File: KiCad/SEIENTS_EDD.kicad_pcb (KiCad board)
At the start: 2 copper layers, 127.1 x 110 mm, 94 parts, among them IC1 A3144EUA, J1 Conn_01x02_Pin, J201 Screw_Terminal_01x04, J3 Screw_Terminal_01x05, J4 Screw_Terminal_01x02, J7 DE9_Socket, J8 DE9_Pins, M4 Motor_DC, M5 Motor_DC, M6 Motor_DC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

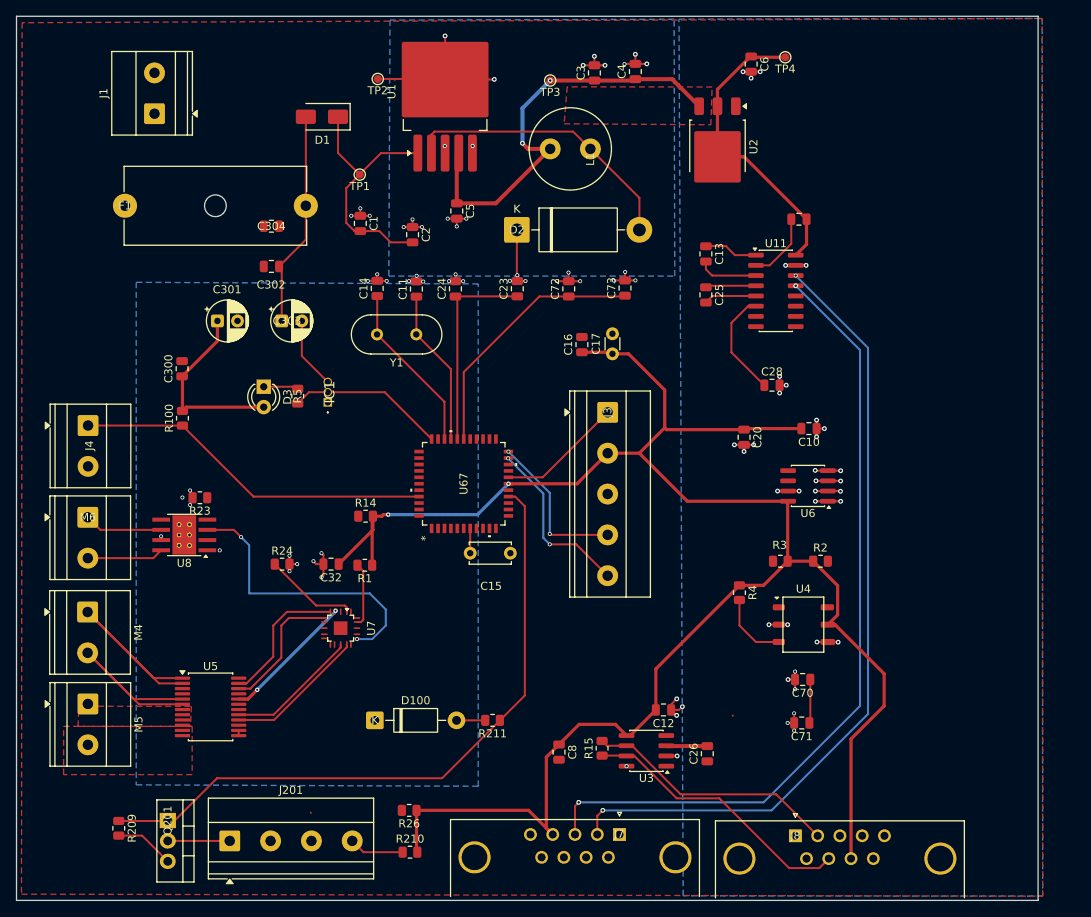
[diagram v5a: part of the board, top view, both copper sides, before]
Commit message: Modificació al routing
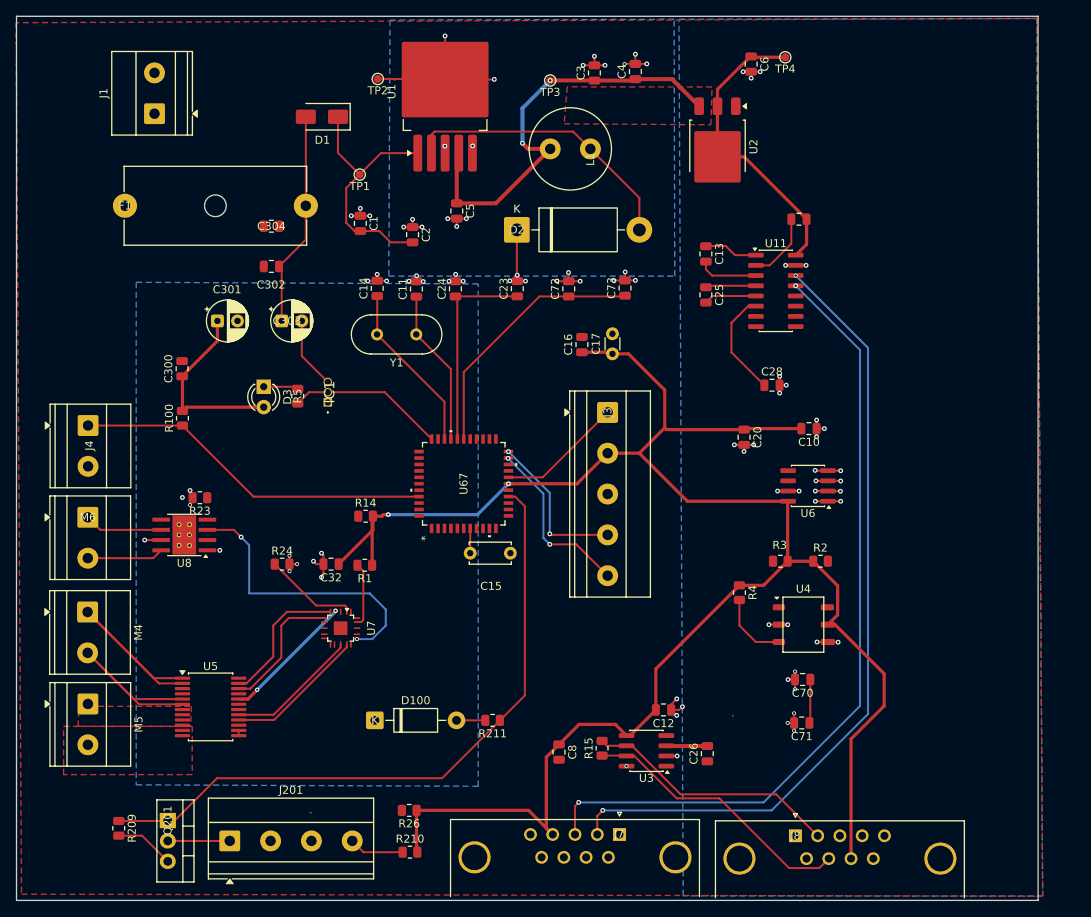
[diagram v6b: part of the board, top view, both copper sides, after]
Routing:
- net GND: track 167.7 -> 168.9 mm
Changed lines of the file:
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@@
 	)
 	(segment
-		(start 128.38 46.225)
-		(end 128.38 45.38)
-		(width 0.25)
-		(layer "F.Cu")
-		(net 1)
-	)
-	(segment
 		(start 174.6 80.5)
 		(end 174.6 81.515)
@@
 	)
 	(segment
+		(start 93.05 94.37)
+		(end 91 94.37)
+		(width 0.25)
+		(layer "F.Cu")
+		(net 1)
+	)
+	(segment
 		(start 128.305 37)
 		(end 128.38 37.075)
@@
 	(via
 		(at 123.225 55.425)
-		(size 0.5)
+		(size 0.6)
 		(drill 0.3)
 		(layers "F.Cu" "B.Cu")
@@
 	(via
 		(at 124.832599 61.482599)
-		(size 0.5)
+		(size 0.6)
 		(drill 0.3)
 		(layers "F.Cu" "B.Cu")
@@
 	(via
 		(at 152.057599 62.062599)
-		(size 0.5)
+		(size 0.6)
 		(drill 0.3)
 		(layers "F.Cu" "B.Cu")
@@
 	(via
 		(at 121.107599 62.132599)
-		(size 0.5)
+		(size 0.6)
 		(drill 0.3)
 		(layers "F.Cu" "B.Cu")
@@
 	(via
 		(at 131.025 54.375)
-		(size 0.5)
+		(size 0.6)
 		(drill 0.3)
 		(layers "F.Cu" "B.Cu")
@@
 	)
 	(via
-		(at 93.045 93.9)
-		(size 0.5)
+		(at 91 94.37)
+		(size 0.6)
 		(drill 0.3)
 		(layers "F.Cu" "B.Cu")
@@
 	(via
 		(at 129.83 55.35)
-		(size 0.5)
+		(size 0.6)
 		(drill 0.3)
 		(layers "F.Cu" "B.Cu")
@@
 	(via
 		(at 119 54.025)
-		(size 0.5)
+		(size 0.6)
 		(drill 0.3)
 		(layers "F.Cu" "B.Cu")
@@
 	(via
 		(at 125.657599 62.207599)
-		(size 0.5)
+		(size 0.6)
 		(drill 0.3)
 		(layers "F.Cu" "B.Cu")
@@
 	(via
 		(at 131.8 45.325)
-		(size 0.5)
+		(size 0.6)
 		(drill 0.3)
 		(layers "F.Cu" "B.Cu")
@@
 	(via
 		(at 128.7 54.375)
-		(size 0.5)
+		(size 0.6)
 		(drill 0.3)
 		(layers "F.Cu" "B.Cu")
@@
 	(via
 		(at 128.35 45.35)
-		(size 0.5)
+		(size 0.6)
 		(drill 0.3)
 		(layers "F.Cu" "B.Cu")
@@
 	(via
 		(at 113 99)
-		(size 0.5)
+		(size 0.6)
 		(drill 0.3)
 		(layers "F.Cu" "B.Cu")
@@
 	(via
 		(at 149.382599 62.087599)
-		(size 0.5)
+		(size 0.6)
 		(drill 0.3)
 		(layers "F.Cu" "B.Cu")
@@
 	(via
 		(at 137.357599 61.412599)
-		(size 0.5)
+		(size 0.6)
 		(drill 0.3)
 		(layers "F.Cu" "B.Cu")
@@
 	(via
 		(at 116.7 54.025)
-		(size 0.5)
+		(size 0.6)
 		(drill 0.3)
 		(layers "F.Cu" "B.Cu")
@@
 	(via
 		(at 96.645 88.2)
-		(size 0.5)
+		(size 0.6)
 		(drill 0.3)
 		(layers "F.Cu" "B.Cu")
@@
 	(via
 		(at 119.932599 61.307599)
-		(size 0.5)
+		(size 0.6)
 		(drill 0.3)
 		(layers "F.Cu" "B.Cu")
@@
 	(via
 		(at 145.182599 62.162599)
-		(size 0.5)
+		(size 0.6)
 		(drill 0.3)
 		(layers "F.Cu" "B.Cu")
@@
 	(via
 		(at 142.282599 62.137599)
-		(size 0.5)
+		(size 0.6)
 		(drill 0.3)
 		(layers "F.Cu" "B.Cu")
@@
 	(via
 		(at 143.732599 61.087599)
-		(size 0.5)
+		(size 0.6)
 		(drill 0.3)
 		(layers "F.Cu" "B.Cu")
@@
 	(via
 		(at 118.757599 62.132599)
-		(size 0.5)
+		(size 0.6)
 		(drill 0.3)
 		(layers "F.Cu" "B.Cu")
@@
 	(via
 		(at 130.632599 62.162599)
-		(size 0.5)
+		(size 0.6)
 		(drill 0.3)
 		(layers "F.Cu" "B.Cu")
@@
 	(via
 		(at 150.782599 61.012599)
-		(size 0.5)
+		(size 0.6)
 		(drill 0.3)
 		(layers "F.Cu" "B.Cu")
@@
 	(via
 		(at 117.83 53.1)
-		(size 0.5)
+		(size 0.6)
 		(drill 0.3)
 		(layers "F.Cu" "B.Cu")
@@
 	(via
 		(at 128.857599 62.162599)
-		(size 0.5)
+		(size 0.6)
 		(drill 0.3)
 		(layers "F.Cu" "B.Cu")
@@
 	(via
 		(at 138.382599 62.137599)
-		(size 0.5)
+		(size 0.6)
 		(drill 0.3)
 		(layers "F.Cu" "B.Cu")
@@
 	(via
 		(at 100.345 95.65)
-		(size 0.5)
+		(size 0.6)
 		(drill 0.3)
 		(layers "F.Cu" "B.Cu")
@@
 	(via
 		(at 123.882599 62.157599)
-		(size 0.5)
+		(size 0.6)
 		(drill 0.3)
 		(layers "F.Cu" "B.Cu")
@@
 	(via
 		(at 95.695 89.075)
-		(size 0.5)
+		(size 0.6)
 		(drill 0.3)
 		(layers "F.Cu" "B.Cu")
@@
 	(via
 		(at 124.33 54.475)
-		(size 0.5)
+		(size 0.6)
 		(drill 0.3)
 		(layers "F.Cu" "B.Cu")
@@
 	(via
 		(at 112 97)
-		(size 0.5)
+		(size 0.6)
 		(drill 0.3)
 		(layers "F.Cu" "B.Cu")
@@
 	(via
 		(at 129.682599 61.312599)
-		(size 0.5)
+		(size 0.6)
 		(drill 0.3)
 		(layers "F.Cu" "B.Cu")
@@
 	(via
 		(at 125.5 55.425)
-		(size 0.5)
+		(size 0.6)
 		(drill 0.3)
 		(layers "F.Cu" "B.Cu")
@@
 	(via
 		(at 113 96)
-		(size 0.5)
+		(size 0.6)
 		(drill 0.3)
 		(layers "F.Cu" "B.Cu")
@@
 	(via
 		(at 136.432599 62.112599)
-		(size 0.5)
+		(size 0.6)
 		(drill 0.3)
 		(layers "F.Cu" "B.Cu")
@@
 	(via
 		(at 136.262599 87.3626)
-		(size 0.55)
+		(size 0.6)
 		(drill 0.25)
 		(layers "F.Cu" "B.Cu")
@@
 	(via
 		(at 121.3 91.2)
-		(size 0.55)
+		(size 0.6)
 		(drill 0.25)
 		(layers "F.Cu" "B.Cu")
@@
 	(via
 		(at 136.262599 83.3626)
-		(size 0.5)
+		(size 0.6)
 		(drill 0.3)
 		(layers "F.Cu" "B.Cu")
@@
 	(via
 		(at 141.4 93.6)
-		(size 0.5)
+		(size 0.6)
 		(drill 0.3)
 		(layers "F.Cu" "B.Cu")
@@
 	(via
 		(at 141.4 94.9)
-		(size 0.5)
+		(size 0.6)
 		(drill 0.3)
 		(layers "F.Cu" "B.Cu")
@@
 	(via
 		(at 136.220657 84.204543)
-		(size 0.5)
+		(size 0.6)
 		(drill 0.3)
 		(layers "F.Cu" "B.Cu")
@@
 	(via
 		(at 103 94)
-		(size 0.5)
+		(size 0.6)
 		(drill 0.3)
 		(layers "F.Cu" "B.Cu")
@@
 		(polygon
 			(pts
-				(xy 75.75 30) (xy 75.675 138.425) (xy 202.725 138.675) (xy 202.675 29.475)
+				(xy 75 30) (xy 75.675 138.425) (xy 202.725 138.675) (xy 202 29.475)
 			)
 		)
@@
 		(polygon
 			(pts
-				(xy 157.475 29.575) (xy 202.675 29.475) (xy 202.725 138.675) (xy 158 138.625)
+				(xy 157.475 29.575) (xy 202 29.475) (xy 202.725 138.675) (xy 158 138.625)
 			)
 		)

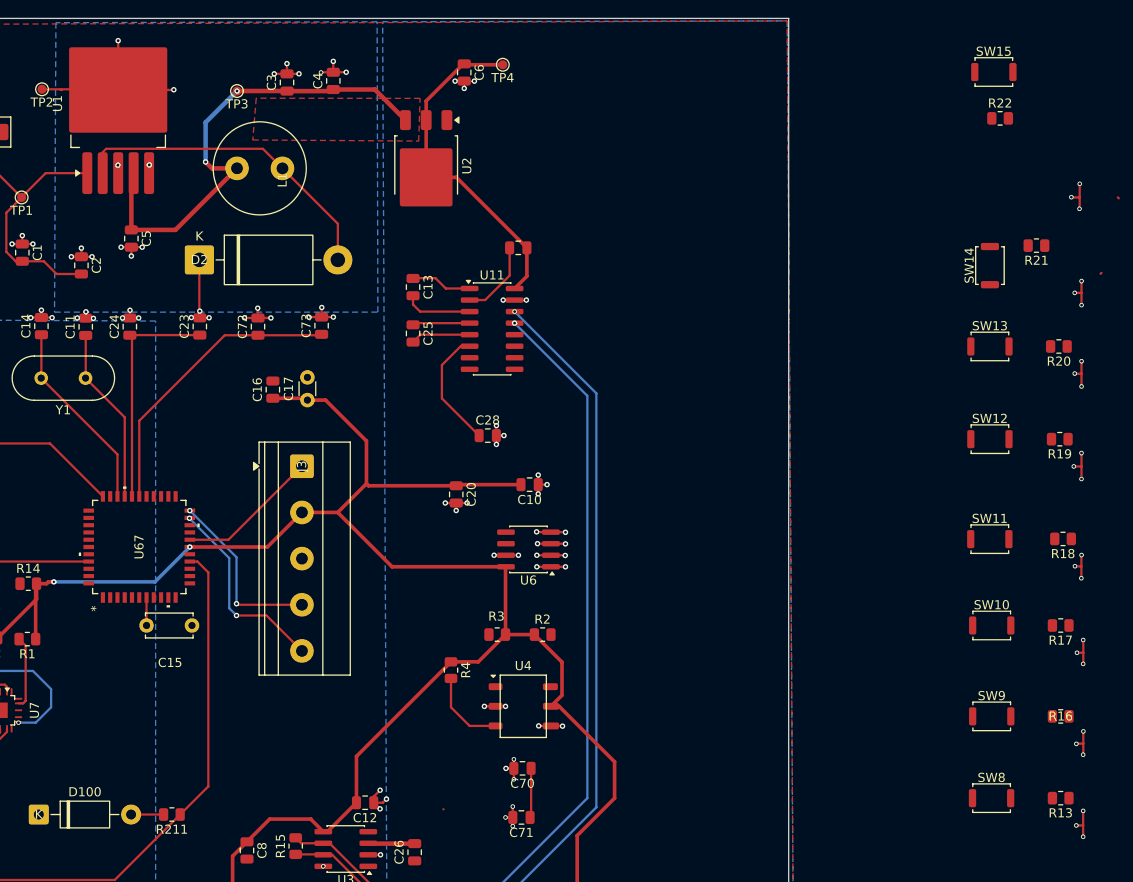
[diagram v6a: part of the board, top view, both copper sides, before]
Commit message: Modificació al routing
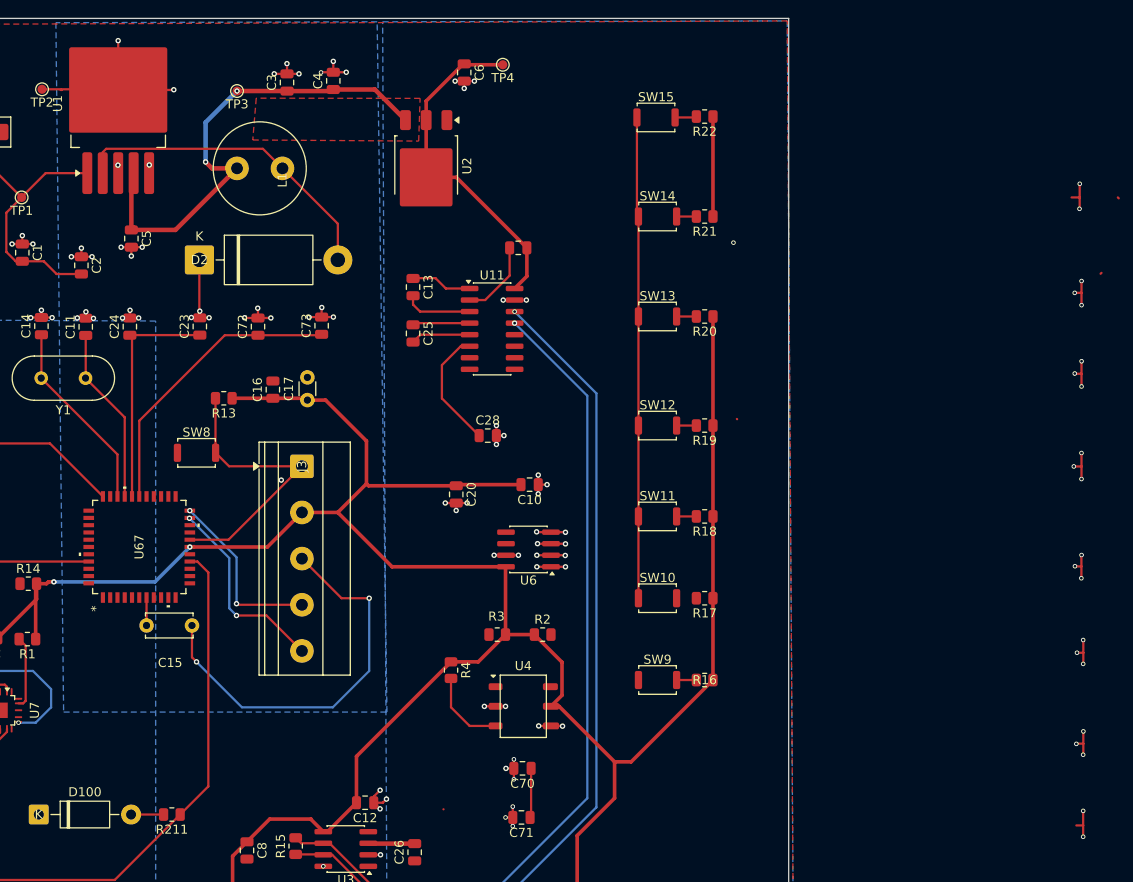
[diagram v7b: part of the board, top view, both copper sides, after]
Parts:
- moved R13 102.1 mm to (140.0, 71.0)
- moved SW8 95.4 mm to (137.0, 77.0)
- moved R18 39.5 mm to (192.9, 84.0)
- moved R16 39.4 mm to (192.9, 102.0)
- moved R17 39.3 mm to (192.9, 93.0)
- moved R20 39.1 mm to (192.9, 62.0)
- moved R19 39.1 mm to (192.9, 74.0)
- moved SW15 37.5 mm to (187.6, 40.1)
- moved SW9 37.0 mm to (187.7, 102.0)
- moved SW14 37.0 mm to (187.7, 51.0), turned to 0 degrees
- moved SW10 36.9 mm to (187.7, 93.0)
- moved SW13 36.7 mm to (187.7, 62.0)
- moved SW11 36.6 mm to (187.7, 84.0)
- moved R21 36.6 mm to (192.9, 51.0)
- moved SW12 36.6 mm to (187.7, 74.0)
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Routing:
- net GND: track 168.9 -> 266.0 mm, vias 111 -> 113
- net +3.3V: track 319.9 -> 389.9 mm
- net Net-(J3-Pin_1): track 15.7 -> 31.8 mm
- net BTN_TEMP_UP: track 0.14 -> 2.53 mm
- net BTN_REC_FWD: track 0.00 -> 2.18 mm
- net BTN_REC_BWD: track 0.14 -> 2.32 mm
- net BTN_POS_FWD: track 0.00 -> 2.18 mm
- net BTN_ALT_UP: track 0.00 -> 2.18 mm
- net BTN_ALT_DN: track 0.00 -> 2.18 mm

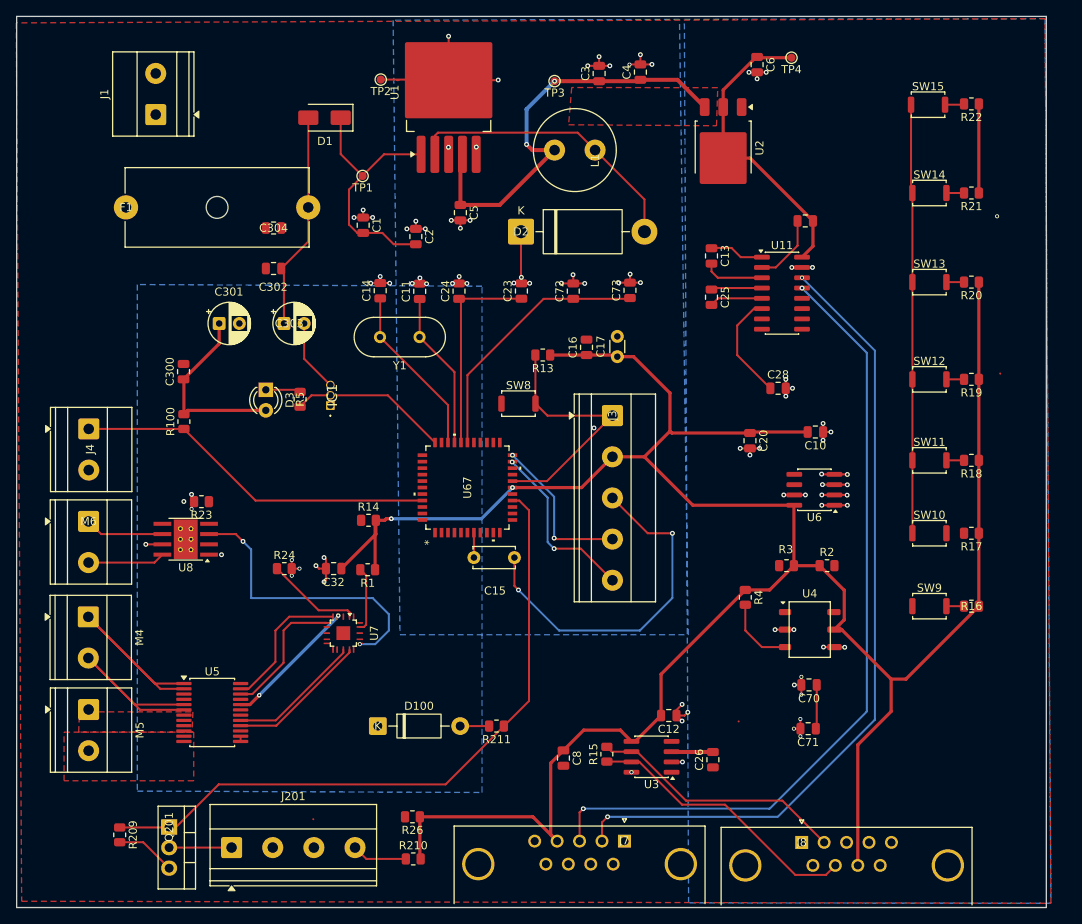
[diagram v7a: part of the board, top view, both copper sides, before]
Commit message: Modificació al routing
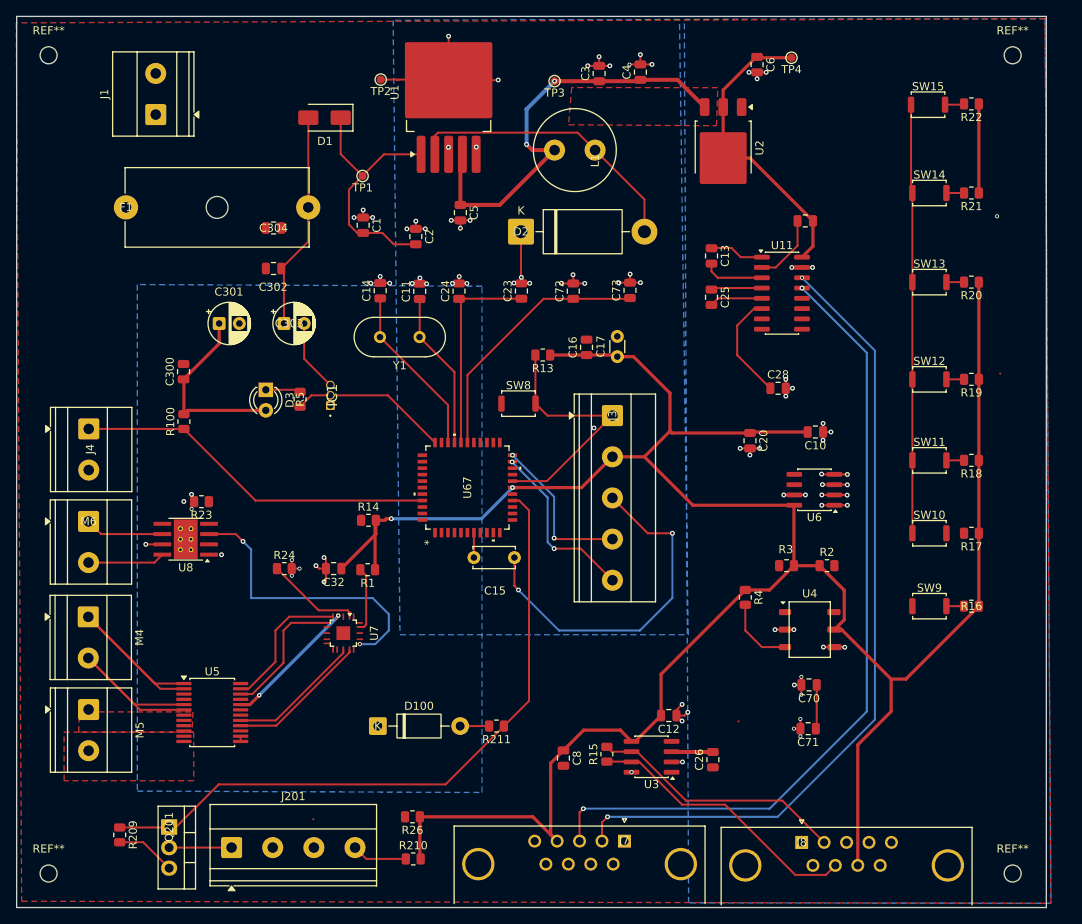
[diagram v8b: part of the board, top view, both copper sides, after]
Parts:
- added REF**: MountingHole_2.1mm, MountingHole:MountingHole_2.1mm, F.Cu at (79.0, 34.0)
- added REF**: MountingHole_2.1mm, MountingHole:MountingHole_2.1mm, F.Cu at (79.0, 135.0)
- added REF**: MountingHole_2.1mm, MountingHole:MountingHole_2.1mm, F.Cu at (198.0, 34.0)
- added REF**: MountingHole_2.1mm, MountingHole:MountingHole_2.1mm, F.Cu at (198.0, 135.0)
